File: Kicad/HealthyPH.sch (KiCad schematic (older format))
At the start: 6 parts, among them P1 CONN_8

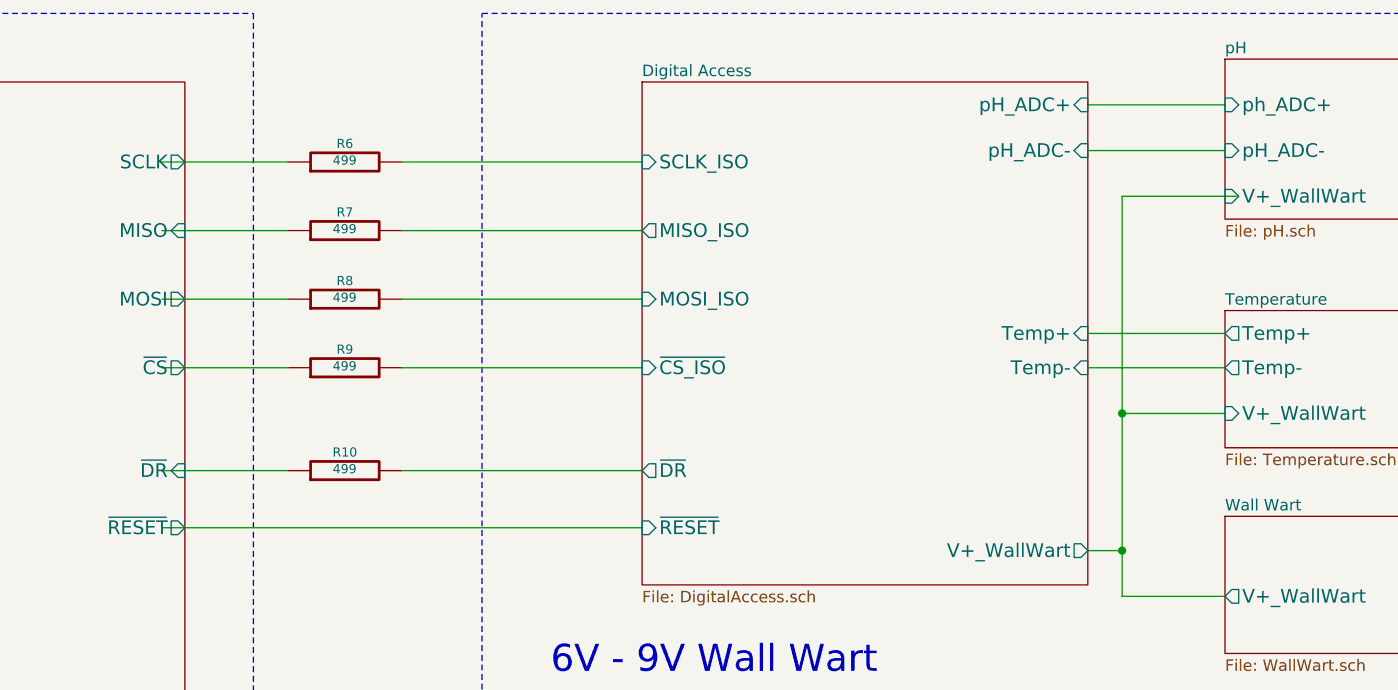
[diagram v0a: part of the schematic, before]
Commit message: Layout with traces - ran through ERC and DRC
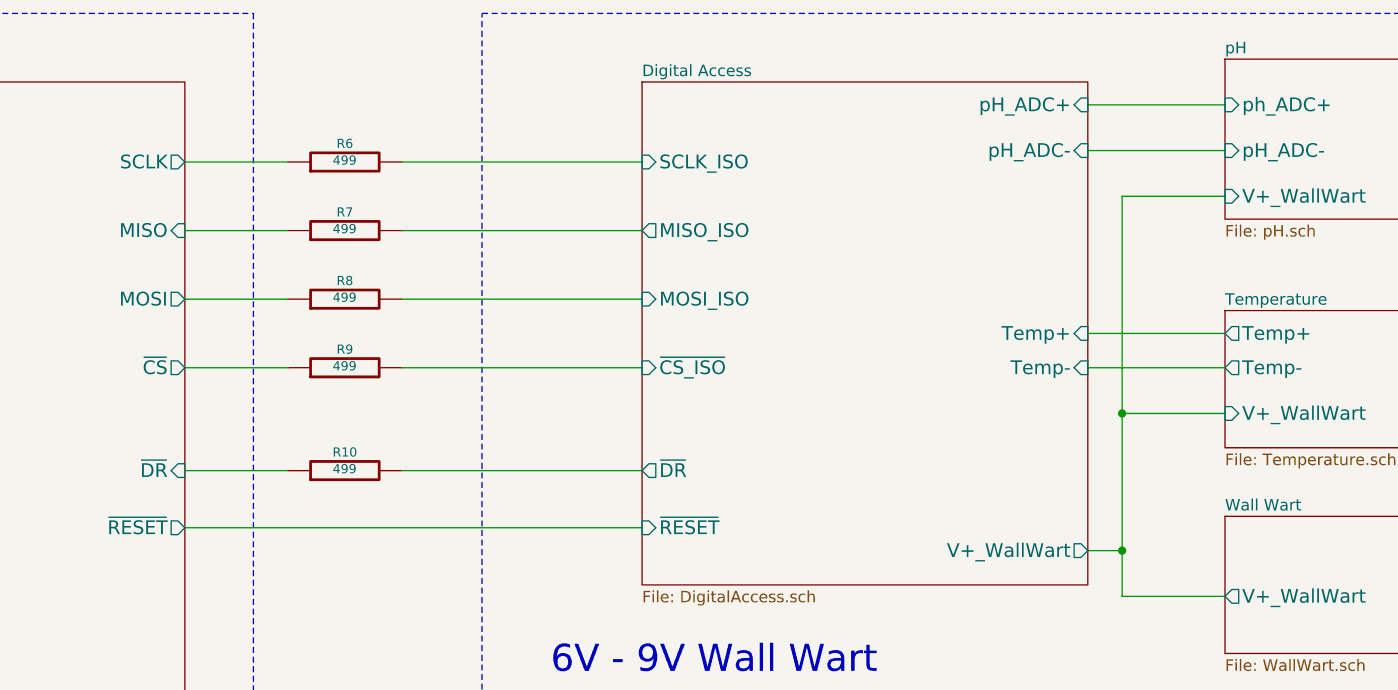
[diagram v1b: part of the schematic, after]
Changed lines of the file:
@@
 Sheet 1 7
 Title ""
-Date "14 aug 2014"
+Date "19 aug 2014"
 Rev ""
 Comp ""
@@
 	7250 2150 6650 2150
 Wire Wire Line
-	7300 1400 6800 1400
-Wire Wire Line
 	7250 2350 6800 2350
 Wire Wire Line
@@
 	6650 2950 6800 2950
 Connection ~ 6800 2950
-Wire Wire Line
-	2600 2850 4700 2850
 Wire Notes Line
 	9950 550  9950 3600
@@
 Wire Wire Line
 	4700 2600 3650 2600
-Wire Wire Line
-	3150 2600 2600 2600
-Wire Wire Line
-	2600 2150 3150 2150
-Wire Wire Line
-	3150 1850 2600 1850
-Wire Wire Line
-	2600 1550 3150 1550
-Wire Wire Line
-	3150 1250 2600 1250
 Wire Wire Line
 	9150 1200 10700 1200
@@
 Wire Wire Line
 	10700 4500 9500 4500
+Wire Wire Line
+	3150 1250 2700 1250
+Wire Wire Line
+	3150 1550 2700 1550
+Wire Wire Line
+	2700 1850 3150 1850
+Wire Wire Line
+	3150 2150 2700 2150
+Wire Wire Line
+	2700 2600 3150 2600
+Wire Wire Line
+	7250 1400 6800 1400
+Wire Wire Line
+	4700 2850 2700 2850
 $EndSCHEMATC

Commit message: Dev Rev 1
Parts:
- added TP2, TP3, TP4, TP5, TP6, TP7: CONN_1, symbol CONN_1
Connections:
- net Arduino/~RESET: now also TP7.1
- net Digital Access/MISO_ISO: now also TP3.1
- net Digital Access/MOSI_ISO: now also TP4.1
- net Digital Access/SCLK_ISO: now also TP2.1
- net Digital Access/~CS_ISO: now also TP5.1
- net Digital Access/~DR: now also TP6.1
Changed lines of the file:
@@
 Sheet 1 7
 Title ""
-Date "20 aug 2014"
+Date "21 aug 2014"
 Rev ""
 Comp ""
@@
 Wire Wire Line
 	4700 2850 2700 2850
+$Comp
+L CONN_1 TP2
+U 1 1 53F5DD37
+P 4250 1000
+F 0 "TP2" H 4330 1000 40  0000 L CNN
+F 1 "CONN_1" H 4250 1055 30  0001 C CNN
+F 2 "" H 4250 1000 60  0000 C CNN
+F 3 "" H 4250 1000 60  0000 C CNN
+	1    4250 1000
+	1    0    0    -1
+$EndComp
+Wire Wire Line
+	4100 1000 4100 1250
+Connection ~ 4100 1250
+$Comp
+L CONN_1 TP3
+U 1 1 53F5DE71
+P 4250 1450
+F 0 "TP3" H 4330 1450 40  0000 L CNN
+F 1 "CONN_1" H 4250 1505 30  0001 C CNN
+F 2 "" H 4250 1450 60  0000 C CNN
+F 3 "" H 4250 1450 60  0000 C CNN
+	1    4250 1450
+	1    0    0    -1
+$EndComp
+Wire Wire Line
+	4100 1450 4100 1550
+Connection ~ 4100 1550
+$Comp
+L CONN_1 TP4
+U 1 1 53F5DF29
+P 4250 1700
+F 0 "TP4" H 4330 1700 40  0000 L CNN
+F 1 "CONN_1" H 4250 1755 30  0001 C CNN
+F 2 "" H 4250 1700 60  0000 C CNN
+F 3 "" H 4250 1700 60  0000 C CNN
+	1    4250 1700
+	1    0    0    -1
+$EndComp
+Wire Wire Line
+	4100 1700 4100 1850
+Connection ~ 4100 1850
+$Comp
+L CONN_1 TP5
+U 1 1 53F5DFE3
+P 4250 2050
+F 0 "TP5" H 4330 2050 40  0000 L CNN
+F 1 "CONN_1" H 4250 2105 30  0001 C CNN
+F 2 "" H 4250 2050 60  0000 C CNN
+F 3 "" H 4250 2050 60  0000 C CNN
+	1    4250 2050
+	1    0    0    -1
+$EndComp
+Wire Wire Line
+	4100 2050 4100 2150
+Connection ~ 4100 2150
+$Comp
+L CONN_1 TP6
+U 1 1 53F5E09F
+P 4300 2450
+F 0 "TP6" H 4380 2450 40  0000 L CNN
+F 1 "CONN_1" H 4300 2505 30  0001 C CNN
+F 2 "" H 4300 2450 60  0000 C CNN
+F 3 "" H 4300 2450 60  0000 C CNN
+	1    4300 2450
+	1    0    0    -1
+$EndComp
+Wire Wire Line
+	4150 2450 4150 2600
+Connection ~ 4150 2600
+$Comp
+L CONN_1 TP7
+U 1 1 53F5E15D
+P 4300 2750
+F 0 "TP7" H 4380 2750 40  0000 L CNN
+F 1 "CONN_1" H 4300 2805 30  0001 C CNN
+F 2 "" H 4300 2750 60  0000 C CNN
+F 3 "" H 4300 2750 60  0000 C CNN
+	1    4300 2750
+	1    0    0    -1
+$EndComp
+Wire Wire Line
+	4150 2750 4150 2850
+Connection ~ 4150 2850
 $EndSCHEMATC

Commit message: updates for dev rev 2
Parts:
- added IC?: LTV-356T, MFSOP6, symbol LTV-356T
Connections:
- wire segments 49 -> 66
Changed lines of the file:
@@
 Sheet 1 7
 Title ""
-Date "21 aug 2014"
+Date "9 sep 2014"
 Rev ""
 Comp ""
@@
 F2 "~RESET" I L 4700 2850 60
 F3 "~DR" O L 4700 2600 60
-F4 "Temp+" I R 6650 2000 60
-F5 "Temp-" I R 6650 2150 60
-F6 "pH_ADC+" I R 6650 1000 60
-F7 "pH_ADC-" I R 6650 1200 60
-F8 "V+_WallWart" O R 6650 2950 60
-F9 "MOSI_ISO" I L 4700 1850 60
-F10 "MISO_ISO" O L 4700 1550 60
-F11 "SCLK_ISO" I L 4700 1250 60
-F12 "~CS_ISO" I L 4700 2150 60
+F4 "pH_ADC+" I R 6650 1000 60
+F5 "pH_ADC-" I R 6650 1200 60
+F6 "V+_WallWart" O R 6650 2950 60
+F7 "MOSI_ISO" I L 4700 1850 60
+F8 "MISO_ISO" O L 4700 1550 60
+F9 "SCLK_ISO" I L 4700 1250 60
+F10 "~CS_ISO" I L 4700 2150 60
+F11 "EC_ADC+" I R 6650 1900 60
+F12 "EC_ADC-" I R 6650 2100 60
 $EndSheet
 $Sheet
@@
 F0 "pH" 50
 F1 "pH.sch" 50
-F2 "ph_ADC+" I L 7250 1000 60
-F3 "pH_ADC-" I L 7250 1200 60
-F4 "V+_WallWart" I L 7250 1400 60
-F5 "pH_V+(in)" I R 9150 1100 60
-F6 "pH_VGND" I R 9150 1200 60
+F2 "V+_WallWart" I L 7250 1400 60
+F3 "ph_ADC_IN+" I L 7250 1000 60
+F4 "pH_ADC_IN-" I L 7250 1200 60
+F5 "pH_PROBE_V" I R 9150 1100 60
+F6 "pH_PROBE_GND" I R 9150 1200 60
 $EndSheet
 $Sheet
@@
 F10 "PumpUp" O R 2700 4350 60
 F11 "PumpDown" O R 2700 4600 60
+F12 "TempV" I R 2700 3750 60
 $EndSheet
 Text Notes 2900 4900 0    118  ~ 0
@@
 F1 "Temperature.sch" 50
 F2 "V+_WallWart" I L 7250 2350 60
-F3 "Temp+" O L 7250 2000 60
-F4 "Temp-" O L 7250 2150 60
-F5 "Temp" O R 9150 2350 60
-F6 "pH_V+" I R 9150 2150 60
+F3 "TempR" I R 9150 2150 60
+F4 "TempV" O L 7250 2150 60
+F5 "AGND" I R 9150 2350 60
 $EndSheet
 $Sheet
@@
 F9 "V+_UpPump" I R 9500 4350 60
 $EndSheet
-Wire Wire Line
-	6650 1000 7250 1000
-Wire Wire Line
-	6650 1200 7250 1200
-Wire Wire Line
-	6650 2000 7250 2000
-Wire Wire Line
-	7250 2150 6650 2150
-Wire Wire Line
-	7250 2350 6800 2350
-Wire Wire Line
-	6800 1400 6800 3150
-Wire Wire Line
-	6800 3150 7250 3150
-Connection ~ 6800 2350
-Wire Wire Line
-	6650 2950 6800 2950
-Connection ~ 6800 2950
-Wire Notes Line
-	9950 550  9950 3600
-Wire Notes Line
-	9950 3600 4000 3600
-Wire Notes Line
-	4000 3600 4000 600
-Wire Notes Line
-	4000 600  9950 600
-Wire Notes Line
-	3000 600  3000 3700
-Wire Notes Line
-	3000 3700 9950 3700
-Wire Notes Line
-	9950 3700 9950 5000
-Wire Notes Line
-	9950 5000 600  5000
-Wire Notes Line
-	600  5000 600  600
-Wire Notes Line
-	600  600  3000 600
-Wire Wire Line
-	3650 1250 4700 1250
-Wire Wire Line
-	3650 1550 4700 1550
-Wire Wire Line
-	4700 1850 3650 1850
-Wire Wire Line
-	3650 2150 4700 2150
-Wire Wire Line
-	4700 2600 3650 2600
-Wire Wire Line
-	9150 1200 10700 1200
-Wire Wire Line
-	9150 2150 10000 2150
-Wire Wire Line
-	10000 2150 10000 1300
-Wire Wire Line
-	10000 1300 10700 1300
-Wire Wire Line
-	9150 2350 10100 2350
-Wire Wire Line
-	10100 2350 10100 1400
-Wire Wire Line
-	10100 1400 10700 1400
-Wire Wire Line
-	10700 1100 9150 1100
-Wire Wire Line
-	10300 1500 10300 4000
-Wire Wire Line
-	10300 1500 10700 1500
-Wire Wire Line
-	10700 1600 10450 1600
-Wire Wire Line
-	10450 1600 10450 4150
-Wire Wire Line
-	2700 3900 7300 3900
-Wire Wire Line
-	2700 4100 7300 4100
-Wire Wire Line
-	2700 4350 7300 4350
-Wire Wire Line
-	2700 4600 7300 4600
 $Comp
 L CONN_8 P1
@@
 	1    0    0    -1
 $EndComp
-Wire Wire Line
-	10300 4000 9500 4000
-Wire Wire Line
-	10450 4150 9500 4150
-Wire Wire Line
-	10700 1700 10600 1700
-Wire Wire Line
-	10600 1700 10600 4350
-Wire Wire Line
-	10600 4350 9500 4350
-Wire Wire Line
-	10700 1800 10700 4500
-Wire Wire Line
-	10700 4500 9500 4500
-Wire Wire Line
-	3150 1250 2700 1250
-Wire Wire Line
-	3150 1550 2700 1550
-Wire Wire Line
-	2700 1850 3150 1850
-Wire Wire Line
-	3150 2150 2700 2150
-Wire Wire Line
-	2700 2600 3150 2600
-Wire Wire Line
-	7250 1400 6800 1400
-Wire Wire Line
-	4700 2850 2700 2850
 $Comp
 L CONN_1 TP2
@@
 	1    0    0    -1
 $EndComp
-Wire Wire Line
-	4100 1000 4100 1250
-Connection ~ 4100 1250
 $Comp
 L CONN_1 TP3
@@
 	1    0    0    -1
 $EndComp
-Wire Wire Line
-	4100 1450 4100 1550
-Connection ~ 4100 1550
 $Comp
 L CONN_1 TP4
@@
 	1    0    0    -1
 $EndComp
-Wire Wire Line
-	4100 1700 4100 1850
-Connection ~ 4100 1850
 $Comp
 L CONN_1 TP5
@@
 	1    0    0    -1
 $EndComp
-Wire Wire Line
-	4100 2050 4100 2150
-Connection ~ 4100 2150
 $Comp
 L CONN_1 TP6
@@
 	1    0    0    -1
 $EndComp
-Wire Wire Line
-	4150 2450 4150 2600
-Connection ~ 4150 2600
 $Comp
 L CONN_1 TP7
@@
 	1    0    0    -1
 $EndComp
+$Comp
+L LTV-356T IC?
+U 1 1 540E0911
+P 6500 3400
+F 0 "IC?" H 6286 3579 40  0000 C CNN
+F 1 "LTV-356T" H 6605 3215 40  0000 C CNN
+F 2 "MFSOP6" H 6336 3225 29  0000 C CNN
+F 3 "" H 6500 3400 60  0000 C CNN
+	1    6500 3400
+	1    0    0    -1
+$EndComp
+Wire Wire Line
+	6650 1000 7250 1000
+Wire Wire Line
+	6650 1200 7250 1200
+Wire Wire Line
+	7250 2350 6800 2350
+Wire Wire Line
+	6800 1400 6800 2350
+Wire Wire Line
+	6800 2350 6800 2950
+Wire Wire Line
+	6800 2950 6800 3150
+Wire Wire Line
+	6800 3150 7250 3150
+Connection ~ 6800 2350
+Wire Wire Line
+	6650 2950 6800 2950
+Connection ~ 6800 2950
+Wire Notes Line
+	9950 550  9950 3600
+Wire Notes Line
+	9950 3600 4000 3600
+Wire Notes Line
+	4000 3600 4000 600
+Wire Notes Line
+	4000 600  9950 600
+Wire Notes Line
+	3000 600  3000 3700
+Wire Notes Line
+	3000 3700 9950 3700
+Wire Notes Line
+	9950 3700 9950 5000
+Wire Notes Line
+	9950 5000 600  5000
+Wire Notes Line
+	600  5000 600  600
+Wire Notes Line
+	600  600  3000 600
+Wire Wire Line
+	3650 1250 4100 1250
+Wire Wire Line
+	4100 1250 4700 1250
+Wire Wire Line
+	3650 1550 4100 1550
+Wire Wire Line
+	4100 1550 4700 1550
+Wire Wire Line
+	3650 1850 4100 1850
+Wire Wire Line
+	4100 1850 4700 1850
+Wire Wire Line
+	3650 2150 4100 2150
+Wire Wire Line
+	4100 2150 4700 2150
+Wire Wire Line
+	3650 2600 4150 2600
+Wire Wire Line
+	4150 2600 4700 2600
+Wire Wire Line
+	9150 1200 10700 1200
+Wire Wire Line
+	9150 2150 10000 2150
+Wire Wire Line
+	10000 2150 10000 1300
+Wire Wire Line
+	10000 1300 10700 1300
+Wire Wire Line
+	10700 1100 9150 1100
+Wire Wire Line
+	10300 1500 10300 4000
+Wire Wire Line
+	10300 1500 10700 1500
+Wire Wire Line
+	10700 1600 10450 1600
+Wire Wire Line
+	10450 1600 10450 4150
+Wire Wire Line
+	2700 3900 7300 3900
+Wire Wire Line
+	2700 4100 6150 4100
+Wire Wire Line
+	6150 4100 7300 4100
+Wire Wire Line
+	2700 4350 7300 4350
+Wire Wire Line
+	2700 4600 7300 4600
+Wire Wire Line
+	10300 4000 9500 4000
+Wire Wire Line
+	10450 4150 9500 4150
+Wire Wire Line
+	10700 1700 10600 1700
+Wire Wire Line
+	10600 1700 10600 4350
+Wire Wire Line
+	10600 4350 9500 4350
+Wire Wire Line
+	10700 1800 10700 4500
+Wire Wire Line
+	10700 4500 9500 4500
+Wire Wire Line
+	3150 1250 2700 1250
+Wire Wire Line
+	3150 1550 2700 1550
+Wire Wire Line
+	2700 1850 3150 1850
+Wire Wire Line
+	3150 2150 2700 2150
+Wire Wire Line
+	2700 2600 3150 2600
+Wire Wire Line
+	7250 1400 6800 1400
+Wire Wire Line
+	2700 2850 4150 2850
+Wire Wire Line
+	4150 2850 4700 2850
+Wire Wire Line
+	4100 1000 4100 1250
+Connection ~ 4100 1250
+Wire Wire Line
+	4100 1450 4100 1550
+Connection ~ 4100 1550
+Wire Wire Line
+	4100 1700 4100 1850
+Connection ~ 4100 1850
+Wire Wire Line
+	4100 2050 4100 2150
+Connection ~ 4100 2150
+Wire Wire Line
+	4150 2450 4150 2600
+Connection ~ 4150 2600
 Wire Wire Line
 	4150 2750 4150 2850
 Connection ~ 4150 2850
+Wire Wire Line
+	9150 2350 9600 2350
+Wire Wire Line
+	9600 2350 10150 2350
+Wire Wire Line
+	10150 2350 10150 1400
+Wire Wire Line
+	10150 1400 10700 1400
+Wire Wire Line
+	7250 2150 7050 2150
+Wire Wire Line
+	7050 2150 7050 3300
+Wire Wire Line
+	7050 3300 6850 3300
+Wire Wire Line
+	9600 2350 9600 3500
+Wire Wire Line
+	9600 3500 6850 3500
+Connection ~ 9600 2350
+Wire Wire Line
+	6150 3500 6150 4100
+Connection ~ 6150 4100
+Wire Wire Line
+	4100 3750 2700 3750
+Wire Wire Line
+	4100 3300 4100 3750
+Wire Wire Line
+	4100 3300 6150 3300
 $EndSCHEMATC

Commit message: Ready for Schematic Design Review
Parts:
- removed IC?: LTV-356T, MFSOP6, symbol LTV-356T
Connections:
- wire segments 66 -> 51
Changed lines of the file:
@@
 Sheet 1 7
 Title ""
-Date "9 sep 2014"
+Date "10 sep 2014"
 Rev ""
 Comp ""
@@
 Comment4 ""
 $EndDescr
-$Sheet
-S 4700 900  1950 2200
-U 53CA7F21
-F0 "Digital Access" 50
-F1 "DigitalAccess.sch" 50
-F2 "~RESET" I L 4700 2850 60
-F3 "~DR" O L 4700 2600 60
-F4 "pH_ADC+" I R 6650 1000 60
-F5 "pH_ADC-" I R 6650 1200 60
-F6 "V+_WallWart" O R 6650 2950 60
-F7 "MOSI_ISO" I L 4700 1850 60
-F8 "MISO_ISO" O L 4700 1550 60
-F9 "SCLK_ISO" I L 4700 1250 60
-F10 "~CS_ISO" I L 4700 2150 60
-F11 "EC_ADC+" I R 6650 1900 60
-F12 "EC_ADC-" I R 6650 2100 60
-$EndSheet
-$Sheet
-S 7250 800  1900 700
-U 53C9635B
-F0 "pH" 50
-F1 "pH.sch" 50
-F2 "V+_WallWart" I L 7250 1400 60
-F3 "ph_ADC_IN+" I L 7250 1000 60
-F4 "pH_ADC_IN-" I L 7250 1200 60
-F5 "pH_PROBE_V" I R 9150 1100 60
-F6 "pH_PROBE_GND" I R 9150 1200 60
-$EndSheet
 $Sheet
 S 7250 2800 1950 600
@@
 F10 "PumpUp" O R 2700 4350 60
 F11 "PumpDown" O R 2700 4600 60
-F12 "TempV" I R 2700 3750 60
 $EndSheet
 Text Notes 2900 4900 0    118  ~ 0
@@
 F1 "Temperature.sch" 50
 F2 "V+_WallWart" I L 7250 2350 60
-F3 "TempR" I R 9150 2150 60
-F4 "TempV" O L 7250 2150 60
-F5 "AGND" I R 9150 2350 60
+F3 "V+_Therm" I R 9150 2350 60
+F4 "10K Therm" I R 9150 2150 60
+F5 "Therm+" O L 7250 2050 60
+F6 "Therm-" O L 7250 2200 60
 $EndSheet
 $Sheet
@@
 	1    0    0    -1
 $EndComp
-$Comp
-L LTV-356T IC?
-U 1 1 540E0911
-P 6500 3400
-F 0 "IC?" H 6286 3579 40  0000 C CNN
-F 1 "LTV-356T" H 6605 3215 40  0000 C CNN
-F 2 "MFSOP6" H 6336 3225 29  0000 C CNN
-F 3 "" H 6500 3400 60  0000 C CNN
-	1    6500 3400
-	1    0    0    -1
-$EndComp
 Wire Wire Line
 	6650 1000 7250 1000
@@
 	7250 2350 6800 2350
 Wire Wire Line
-	6800 1400 6800 2350
-Wire Wire Line
-	6800 2350 6800 2950
-Wire Wire Line
-	6800 2950 6800 3150
+	6800 1400 6800 3150
 Wire Wire Line
 	6800 3150 7250 3150
@@
 	600  600  3000 600
 Wire Wire Line
-	3650 1250 4100 1250
-Wire Wire Line
-	4100 1250 4700 1250
-Wire Wire Line
-	3650 1550 4100 1550
-Wire Wire Line
-	4100 1550 4700 1550
-Wire Wire Line
-	3650 1850 4100 1850
-Wire Wire Line
-	4100 1850 4700 1850
-Wire Wire Line
-	3650 2150 4100 2150
-Wire Wire Line
-	4100 2150 4700 2150
-Wire Wire Line
-	3650 2600 4150 2600
-Wire Wire Line
-	4150 2600 4700 2600
+	3650 1250 4700 1250
+Wire Wire Line
+	3650 1550 4700 1550
+Wire Wire Line
+	3650 1850 4700 1850
+Wire Wire Line
+	3650 2150 4700 2150
+Wire Wire Line
+	3650 2600 4700 2600
 Wire Wire Line
 	9150 1200 10700 1200
@@
 	10000 1300 10700 1300
 Wire Wire Line
-	10700 1100 9150 1100
-Wire Wire Line
 	10300 1500 10300 4000
 Wire Wire Line
@@
 	2700 3900 7300 3900
 Wire Wire Line
-	2700 4100 6150 4100
-Wire Wire Line
-	6150 4100 7300 4100
+	2700 4100 7300 4100
 Wire Wire Line
 	2700 4350 7300 4350
@@
 	7250 1400 6800 1400
 Wire Wire Line
-	2700 2850 4150 2850
-Wire Wire Line
-	4150 2850 4700 2850
+	2700 2850 4700 2850
 Wire Wire Line
 	4100 1000 4100 1250
@@
 Connection ~ 4150 2850
 Wire Wire Line
-	9150 2350 9600 2350
-Wire Wire Line
-	9600 2350 10150 2350
+	9150 2350 10150 2350
 Wire Wire Line
 	10150 2350 10150 1400
 Wire Wire Line
 	10150 1400 10700 1400
-Wire Wire Line
-	7250 2150 7050 2150
-Wire Wire Line
-	7050 2150 7050 3300
-Wire Wire Line
-	7050 3300 6850 3300
-Wire Wire Line
-	9600 2350 9600 3500
-Wire Wire Line
-	9600 3500 6850 3500
-Connection ~ 9600 2350
-Wire Wire Line
-	6150 3500 6150 4100
-Connection ~ 6150 4100
-Wire Wire Line
-	4100 3750 2700 3750
-Wire Wire Line
-	4100 3300 4100 3750
-Wire Wire Line
-	4100 3300 6150 3300
+$Sheet
+S 7250 800  1900 700
+U 53C9635B
+F0 "pH" 50
+F1 "pH.sch" 50
+F2 "V+_WallWart" I L 7250 1400 60
+F3 "ph_ADC_IN+" I L 7250 1000 60
+F4 "pH_ADC_IN-" I L 7250 1200 60
+F5 "pH_Probe_V" I R 9150 1000 60
+F6 "pH_Probe_GND" I R 9150 1200 60
+$EndSheet
+Wire Wire Line
+	9150 1000 10600 1000
+Wire Wire Line
+	10600 1000 10600 1100
+Wire Wire Line
+	10600 1100 10700 1100
+$Sheet
+S 4700 900  1950 2200
+U 53CA7F21
+F0 "Digital Access" 50
+F1 "DigitalAccess.sch" 50
+F2 "~RESET" I L 4700 2850 60
+F3 "~DR" O L 4700 2600 60
+F4 "pH_ADC+" I R 6650 1000 60
+F5 "pH_ADC-" I R 6650 1200 60
+F6 "V+_WallWart" O R 6650 2950 60
+F7 "MOSI_ISO" I L 4700 1850 60
+F8 "MISO_ISO" O L 4700 1550 60
+F9 "SCLK_ISO" I L 4700 1250 60
+F10 "~CS_ISO" I L 4700 2150 60
+F11 "Therm+" I R 6650 2050 60
+F12 "Therm-" I R 6650 2200 60
+$EndSheet
+Wire Wire Line
+	6650 2200 7250 2200
+Wire Wire Line
+	6650 2050 7250 2050
 $EndSCHEMATC

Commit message: Layout ready for final check prior to PCB fab
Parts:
- added R16: 499, ~, symbol R
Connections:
- net Temperature/V+_Therm is gone; now on net Digital Access/V+_WallWart: P1.4 (P4)
- net Arduino/~RESET: now also R16.1; no longer TP7.1
- new net Digital Access/~RESET: R16.2, TP7.1
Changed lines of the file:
@@
 Sheet 1 7
 Title ""
-Date "11 sep 2014"
+Date "13 sep 2014"
 Rev ""
 Comp ""
@@
 F0 "Temperature" 50
 F1 "Temperature.sch" 50
-F2 "V+_WallWart" I L 7250 2350 60
-F3 "V+_Therm" I R 9150 2350 60
-F4 "10K Therm" I R 9150 2150 60
-F5 "Therm+" O L 7250 2050 60
-F6 "Therm-" O L 7250 2200 60
+F2 "10K Therm" I R 9150 2150 60
+F3 "Therm+" O L 7250 2050 60
+F4 "Therm-" O L 7250 2200 60
 $EndSheet
 $Sheet
@@
 	6650 1200 7250 1200
 Wire Wire Line
-	7250 2350 6800 2350
-Wire Wire Line
 	6800 1400 6800 3150
 Wire Wire Line
 	6800 3150 7250 3150
-Connection ~ 6800 2350
 Wire Wire Line
 	6650 2950 6800 2950
@@
 	7250 1400 6800 1400
 Wire Wire Line
-	2700 2850 4700 2850
-Wire Wire Line
 	4100 1000 4100 1250
 Connection ~ 4100 1250
@@
 Wire Wire Line
 	4150 2750 4150 2850
-Connection ~ 4150 2850
-Wire Wire Line
-	9150 2350 10150 2350
-Wire Wire Line
-	10150 2350 10150 1400
+Wire Wire Line
+	10150 2600 10150 1400
 Wire Wire Line
 	10150 1400 10700 1400
@@
 Wire Wire Line
 	6650 2050 7250 2050
+$Comp
+L R R16
+U 1 1 54142348
+P 3400 2850
+F 0 "R16" V 3480 2850 40  0000 C CNN
+F 1 "499" V 3407 2851 40  0000 C CNN
+F 2 "~" V 3330 2850 30  0000 C CNN
+F 3 "~" H 3400 2850 30  0000 C CNN
+	1    3400 2850
+	0    -1   -1   0
+$EndComp
+Wire Wire Line
+	2700 2850 3150 2850
+Wire Wire Line
+	3650 2850 4700 2850
+Connection ~ 4150 2850
+Wire Wire Line
+	6800 2600 10150 2600
+Connection ~ 6800 2600
 $EndSCHEMATC
